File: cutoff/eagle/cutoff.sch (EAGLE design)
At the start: 29 parts, among them K1 RELAY, U1 LM2931ADT-5.0RKG, U2 NUD3160, U3 ATMEGA328, Y1 16MHz

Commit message: Ready for final routing.
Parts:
- added C8: 0.1uF, resistor:C-USC0603K
- added D4: MBR0540, cutoff:SMF5.0AT1
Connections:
- removed net CONTROL: U2.G, U3.ADC7
- new net AREF: C8.1, U3.AREF
- new net RELAY: U2.G, U3.PC1(ADC1)
- net +12V: now also D4.C
- net GND: now also C8.2
- net N$1: now also D4.A
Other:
- note added: "A0"
- note added: "D10"
- note added: "D15"
- note added: "GND"
- note added: "TODO: VERIFY FOOTPRINTS"
- note added: "VIN"
- note added: "VOUT_NC"
- note added: "VOUT_NO"
- note removed: "TODO: AREF CAPACITOR"
- note removed: "TODO: FOOTPRINTS"
- note removed: "TODO: MCU PIN SELECTION"
- moved on the sheet: C6, C7, JP4, K1

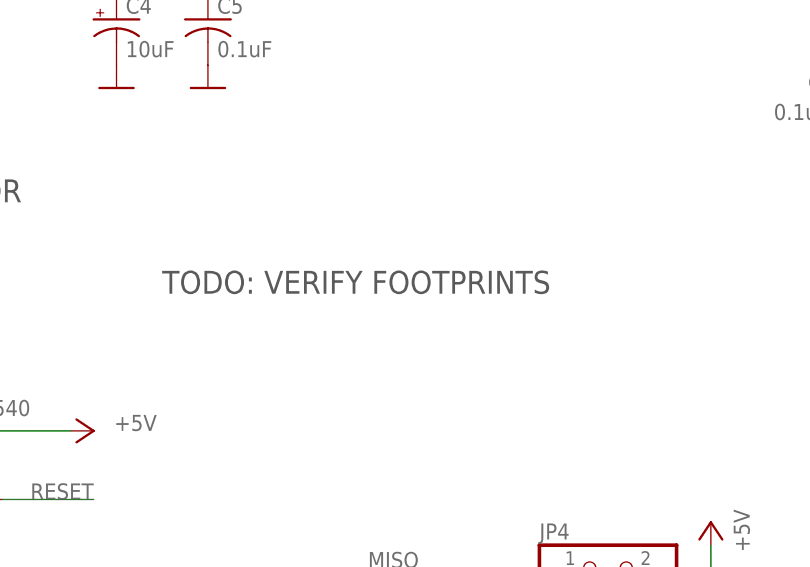
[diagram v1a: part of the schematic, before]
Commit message: Removed TODO from schematic.
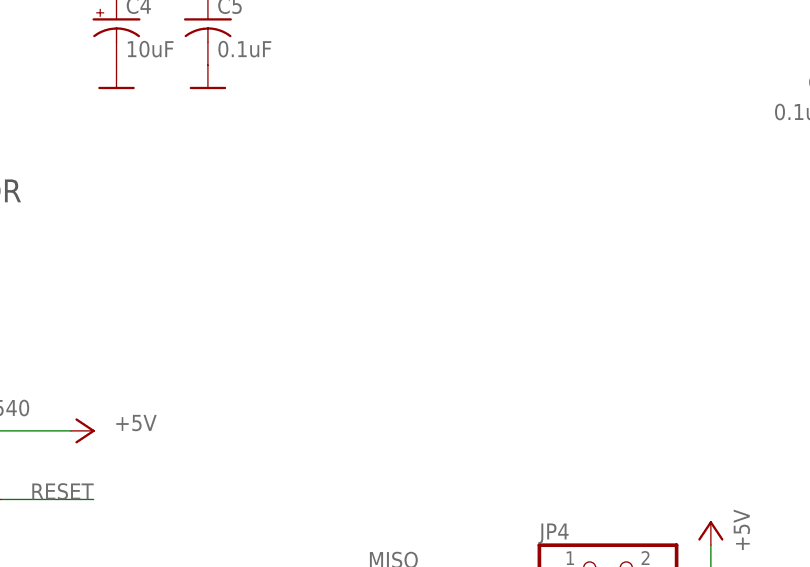
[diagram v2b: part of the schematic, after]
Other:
- note removed: "TODO: VERIFY FOOTPRINTS"
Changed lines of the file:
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@@
 <text x="223.52" y="162.56" size="2.54" layer="97">POWER OUT</text>
 <text x="73.66" y="111.76" size="2.54" layer="97">5V RGULATOR</text>
-<text x="111.76" y="101.6" size="2.54" layer="97">TODO: VERIFY FOOTPRINTS</text>
 <text x="287.02" y="139.7" size="1.778" layer="97">A0</text>
 <text x="287.02" y="137.16" size="1.778" layer="97">D15</text>

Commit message: Completed BOM. Generated library from schematic file.
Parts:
- C1: device beeper:CPOL-USUD-6,3X5,8 -> cutoff:CPOL-USUD-6,3X5,8
- C2, C3, C5, C6, C7, C8: device resistor:C-USC0603K -> cutoff:C-USC0603K
- C4: device beeper:CPOL-USA/3216-18R -> cutoff:CPOL-USA/3216-18R
- D3: device ir-control:LED -> cutoff:LED
- R1, R2, R3, R4, R6: device resistor:R-US_R0402 -> cutoff:R-US_R0402
- R5: value 3K3 -> 1K; device resistor:R-US_R0402 -> cutoff:R-US_R0402
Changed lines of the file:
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@@
 </classes>
 <parts>
-<part name="R5" library="resistor" deviceset="R-US_" device="R0402" value="3K3"/>
+<part name="R5" library="cutoff" deviceset="R-US_" device="R0402" value="1K"/>
 <part name="GND6" library="cutoff" deviceset="GND" device=""/>
-<part name="C2" library="resistor" deviceset="C-US" device="C0603K" value="0.1uF"/>
-<part name="C3" library="resistor" deviceset="C-US" device="C0603K" value="0.1uF"/>
+<part name="C2" library="cutoff" deviceset="C-US" device="C0603K" value="0.1uF"/>
+<part name="C3" library="cutoff" deviceset="C-US" device="C0603K" value="0.1uF"/>
 <part name="P+5" library="cutoff" deviceset="+5V" device=""/>
-<part name="R1" library="resistor" deviceset="R-US_" device="R0402" value="10K"/>
-<part name="R2" library="resistor" deviceset="R-US_" device="R0402" value="10K"/>
+<part name="R1" library="cutoff" deviceset="R-US_" device="R0402" value="10K"/>
+<part name="R2" library="cutoff" deviceset="R-US_" device="R0402" value="10K"/>
 <part name="GND9" library="cutoff" deviceset="GND" device=""/>
 <part name="GND13" library="cutoff" deviceset="GND" device=""/>
@@
 <part name="P+3" library="cutoff" deviceset="+5V" device=""/>
 <part name="GND14" library="cutoff" deviceset="GND" device=""/>
-<part name="R6" library="resistor" deviceset="R-US_" device="R0402" value="10K"/>
+<part name="R6" library="cutoff" deviceset="R-US_" device="R0402" value="10K"/>
 <part name="P+4" library="cutoff" deviceset="+5V" device=""/>
 <part name="JP3" library="cutoff" deviceset="PINHD-1X6" device=""/>
@@
 <part name="Y1" library="cutoff" deviceset="RESONATOR" device="SMD" value="16MHz"/>
 <part name="GND12" library="cutoff" deviceset="GND" device=""/>
-<part name="C1" library="beeper" deviceset="CPOL-US" device="UD-6,3X5,8" value="22uF 40V"/>
-<part name="C5" library="resistor" deviceset="C-US" device="C0603K" value="0.1uF"/>
-<part name="C4" library="beeper" deviceset="CPOL-US" device="A/3216-18R" value="10uF"/>
-<part name="C6" library="resistor" deviceset="C-US" device="C0603K" value="0.1uF"/>
+<part name="C1" library="cutoff" deviceset="CPOL-US" device="UD-6,3X5,8" value="22uF 40V"/>
+<part name="C5" library="cutoff" deviceset="C-US" device="C0603K" value="0.1uF"/>
+<part name="C4" library="cutoff" deviceset="CPOL-US" device="A/3216-18R" value="10uF"/>
+<part name="C6" library="cutoff" deviceset="C-US" device="C0603K" value="0.1uF"/>
 <part name="GND11" library="cutoff" deviceset="GND" device=""/>
 <part name="F1" library="cutoff" deviceset="FUSE" device="" value="500ma Slow"/>
@@
 <part name="NC3" library="cutoff" deviceset="NC" device=""/>
 <part name="K1" library="cutoff" deviceset="RELAY" device="" value="RELAY"/>
-<part name="R3" library="resistor" deviceset="R-US_" device="R0402" value="60K"/>
-<part name="R4" library="resistor" deviceset="R-US_" device="R0402" value="30K"/>
+<part name="R3" library="cutoff" deviceset="R-US_" device="R0402" value="60K"/>
+<part name="R4" library="cutoff" deviceset="R-US_" device="R0402" value="30K"/>
 <part name="GND5" library="cutoff" deviceset="GND" device=""/>
 <part name="JP1" library="cutoff" deviceset="WIRE_PAD" device=""/>
@@
 <part name="GND8" library="cutoff" deviceset="GND" device=""/>
 <part name="P+2" library="cutoff" deviceset="+5V" device=""/>
-<part name="D3" library="ir-control" deviceset="LED" device=""/>
+<part name="D3" library="cutoff" deviceset="LED" device=""/>
 <part name="NC4" library="cutoff" deviceset="NC" device=""/>
 <part name="NC8" library="cutoff" deviceset="NC" device=""/>
@@
 <part name="NC16" library="cutoff" deviceset="NC" device=""/>
 <part name="D1" library="cutoff" deviceset="SMF5.0AT1" device="" value="MBR0540"/>
-<part name="C7" library="resistor" deviceset="C-US" device="C0603K" value="0.1uF"/>
+<part name="C7" library="cutoff" deviceset="C-US" device="C0603K" value="0.1uF"/>
 <part name="GND16" library="cutoff" deviceset="GND" device=""/>
 <part name="NC7" library="cutoff" deviceset="NC" device=""/>
 <part name="NC2" library="cutoff" deviceset="NC" device=""/>
-<part name="C8" library="resistor" deviceset="C-US" device="C0603K" value="0.1uF"/>
+<part name="C8" library="cutoff" deviceset="C-US" device="C0603K" value="0.1uF"/>
 <part name="GND17" library="cutoff" deviceset="GND" device=""/>
 <part name="D4" library="cutoff" deviceset="SMF5.0AT1" device="" value="MBR0540"/>
